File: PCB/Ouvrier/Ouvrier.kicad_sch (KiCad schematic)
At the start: 12 parts, among them J1 Batterie, J2 VBAT Xiao, J3 DC 5V input, Q1 2N2222B, U1 XIAO-ESP32-S3-Plus-DIP, U2 BMP581, U3 UWB

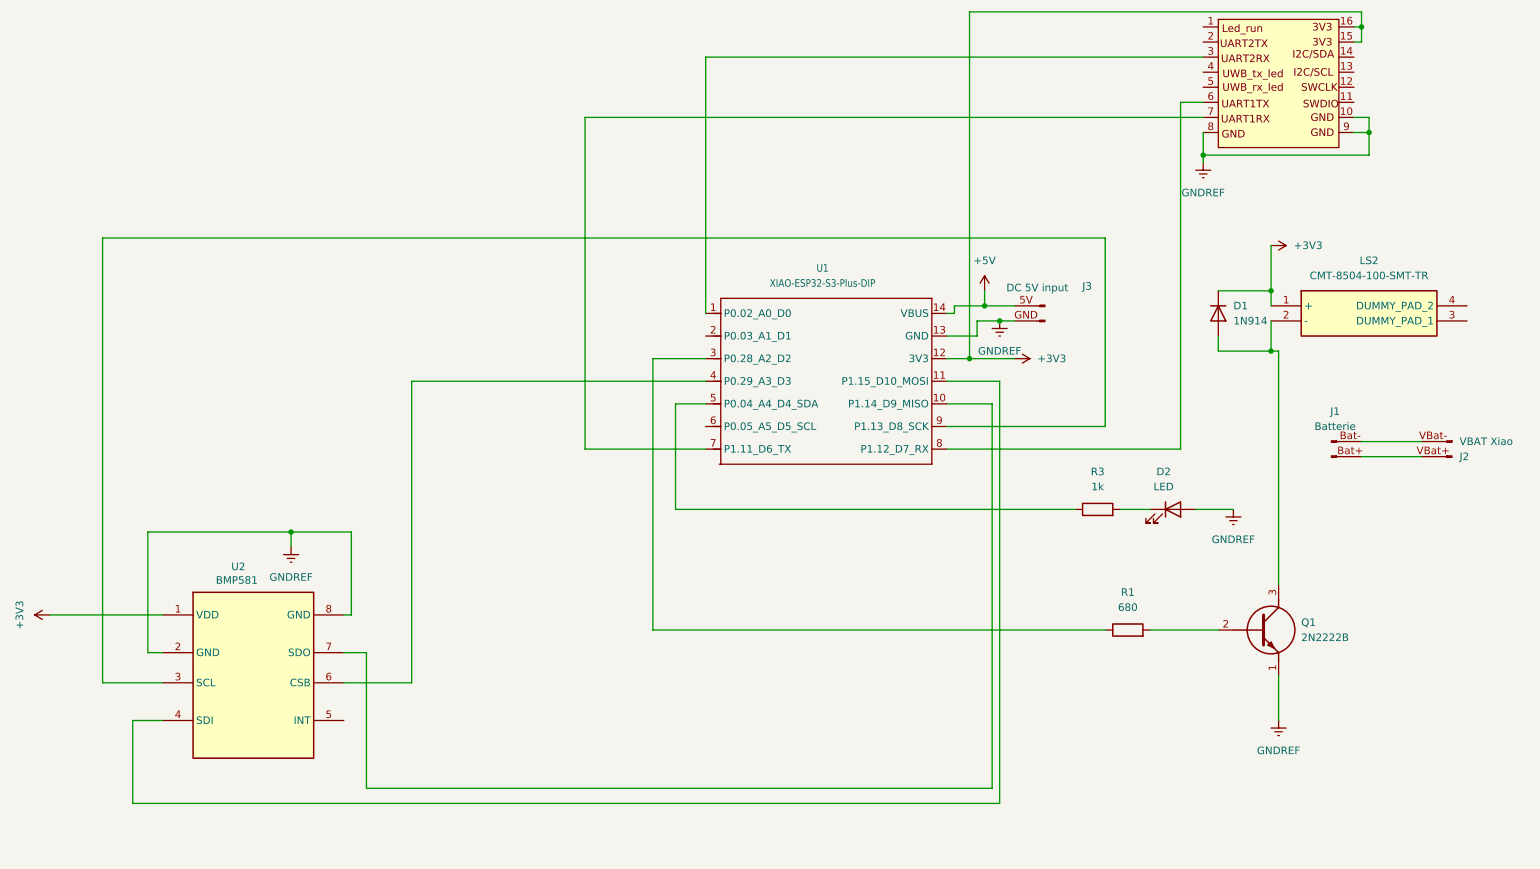
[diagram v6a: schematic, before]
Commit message: MaJ KiCad Ouvrier
pin INT BMP et raccord batterie
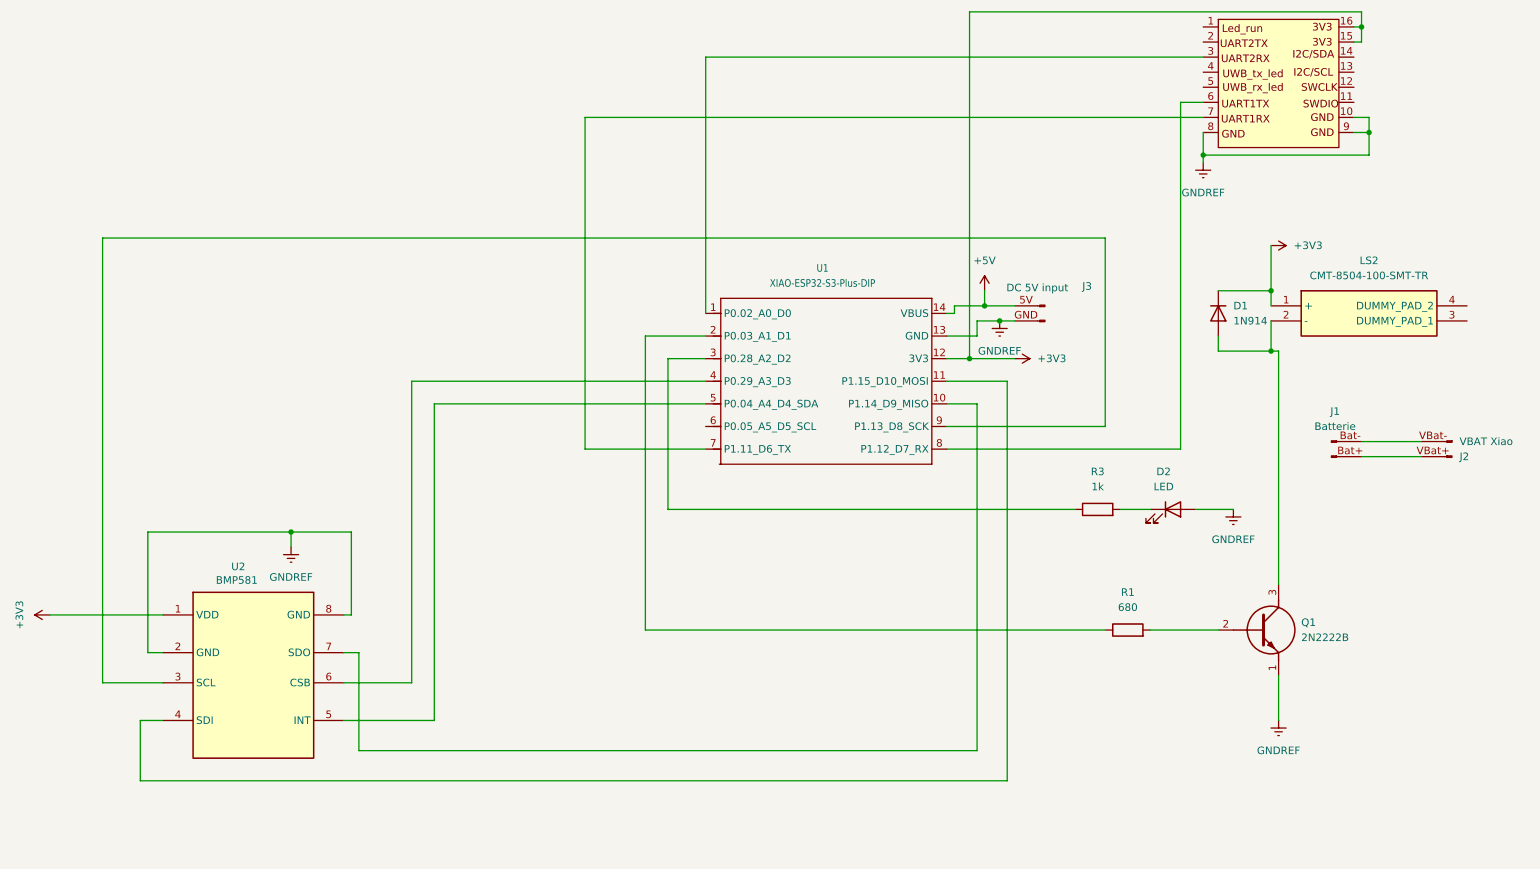
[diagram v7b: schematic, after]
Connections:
- net at R3.1: now also U1.3 (P0.28_A2_D2); no longer U1.5 (P0.04_A4_D4_SDA)
- net at R1.1: now also U1.2 (P0.03_A1_D1); no longer U1.3 (P0.28_A2_D2)
- net at U2.5 (INT): now also U1.5 (P0.04_A4_D4_SDA)
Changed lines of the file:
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@@
 	(wire
 		(pts
-			(xy 189.23 163.83) (xy 83.82 163.83)
+			(xy 186.69 157.48) (xy 82.55 157.48)
 		)
 		(stroke
@@
 	(wire
 		(pts
-			(xy 44.45 166.37) (xy 44.45 152.4)
+			(xy 45.72 162.56) (xy 45.72 152.4)
 		)
 		(stroke
@@
 	(wire
 		(pts
-			(xy 135.89 116.84) (xy 203.2 116.84)
+			(xy 134.62 116.84) (xy 203.2 116.84)
 		)
 		(stroke
@@
 	(wire
 		(pts
-			(xy 140.97 91.44) (xy 132.08 91.44)
-		)
-		(stroke
-			(width 0)
-			(type default)
-		)
-	)
-	(wire
-		(pts
-			(xy 135.89 99.06) (xy 140.97 99.06)
-		)
-		(stroke
-			(width 0)
-			(type default)
-		)
-	)
-	(wire
-		(pts
 			(xy 185.42 33.02) (xy 185.42 91.44)
 		)
@@
 	(wire
 		(pts
-			(xy 83.82 140.97) (xy 83.82 163.83)
-		)
-		(stroke
-			(width 0)
-			(type default)
-		)
-	)
-	(wire
-		(pts
-			(xy 181.61 99.06) (xy 189.23 99.06)
-		)
-		(stroke
-			(width 0)
-			(type default)
-		)
-	)
-	(wire
-		(pts
-			(xy 189.23 99.06) (xy 189.23 163.83)
+			(xy 82.55 140.97) (xy 82.55 157.48)
+		)
+		(stroke
+			(width 0)
+			(type default)
+		)
+	)
+	(wire
+		(pts
+			(xy 181.61 99.06) (xy 186.69 99.06)
+		)
+		(stroke
+			(width 0)
+			(type default)
+		)
+	)
+	(wire
+		(pts
+			(xy 186.69 99.06) (xy 186.69 157.48)
 		)
 		(stroke
@@
 	(wire
 		(pts
-			(xy 135.89 116.84) (xy 135.89 99.06)
-		)
-		(stroke
-			(width 0)
-			(type default)
-		)
-	)
-	(wire
-		(pts
-			(xy 44.45 166.37) (xy 190.5 166.37)
+			(xy 134.62 116.84) (xy 134.62 91.44)
+		)
+		(stroke
+			(width 0)
+			(type default)
+		)
+	)
+	(wire
+		(pts
+			(xy 95.25 99.06) (xy 140.97 99.06)
+		)
+		(stroke
+			(width 0)
+			(type default)
+		)
+	)
+	(wire
+		(pts
+			(xy 45.72 162.56) (xy 191.77 162.56)
 		)
 		(stroke
@@
 	(wire
 		(pts
-			(xy 190.5 95.25) (xy 190.5 166.37)
+			(xy 191.77 95.25) (xy 191.77 162.56)
 		)
 		(stroke
@@
 	(wire
 		(pts
-			(xy 132.08 91.44) (xy 132.08 137.16)
+			(xy 130.81 87.63) (xy 130.81 137.16)
 		)
 		(stroke
@@
 	(wire
 		(pts
+			(xy 95.25 99.06) (xy 95.25 152.4)
+		)
+		(stroke
+			(width 0)
+			(type default)
+		)
+	)
+	(wire
+		(pts
 			(xy 223.52 116.84) (xy 229.87 116.84)
 		)
@@
 	(wire
 		(pts
-			(xy 132.08 137.16) (xy 208.28 137.16)
+			(xy 130.81 137.16) (xy 208.28 137.16)
 		)
 		(stroke
@@
 	(wire
 		(pts
-			(xy 80.01 140.97) (xy 83.82 140.97)
+			(xy 82.55 140.97) (xy 80.01 140.97)
+		)
+		(stroke
+			(width 0)
+			(type default)
+		)
+	)
+	(wire
+		(pts
+			(xy 95.25 152.4) (xy 80.01 152.4)
 		)
 		(stroke
@@
 	(wire
 		(pts
+			(xy 134.62 91.44) (xy 140.97 91.44)
+		)
+		(stroke
+			(width 0)
+			(type default)
+		)
+	)
+	(wire
+		(pts
 			(xy 224.79 57.15) (xy 252.73 57.15)
 		)
@@
 	(wire
 		(pts
+			(xy 130.81 87.63) (xy 140.97 87.63)
+		)
+		(stroke
+			(width 0)
+			(type default)
+		)
+	)
+	(wire
+		(pts
 			(xy 236.22 72.39) (xy 236.22 80.01)
 		)
@@
 	(wire
 		(pts
-			(xy 181.61 95.25) (xy 190.5 95.25)
+			(xy 181.61 95.25) (xy 191.77 95.25)
 		)
 		(stroke
@@
 	(wire
 		(pts
-			(xy 44.45 152.4) (xy 49.53 152.4)
-		)
-		(stroke
+			(xy 45.72 152.4) (xy 49.53 152.4)
+		)
+		(stroke
